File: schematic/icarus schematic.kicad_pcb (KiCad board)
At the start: 2 copper layers, 2 parts, among them U1 ESP32-S3, U2 BMI088

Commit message: added datasheets
other Datasheets

Added capacitors across motors

Added connectors instead of motors.

Add link to mini 100 brushed frame model

Remove URL from Frame file

Update Frame

Delete Frame

Add files via upload

this is the version -1 drone frame

PCB first iteration.
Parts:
- removed U1: ESP32-S3, Package_DFN_QFN:QFN-56-1EP_7x7mm_P0.4mm_EP4x4mm
- added C1: 10uF, Capacitor_SMD:C_0402_1005Metric_Pad0.74x0.62mm_HandSolder, F.Cu at (186.4, 96.0)
- added C10: 0.1uF, Capacitor_SMD:C_0603_1608Metric_Pad1.08x0.95mm_HandSolder, F.Cu at (219.9, 73.0)
- added C11: 0.1uF, Capacitor_SMD:C_0603_1608Metric_Pad1.08x0.95mm_HandSolder, F.Cu at (220.1, 95.5)
- added C12: 0.1uF, Capacitor_SMD:C_0603_1608Metric_Pad1.08x0.95mm_HandSolder, F.Cu at (220.2, 85.8)
- added C13: 0.1uF, Capacitor_SMD:C_0603_1608Metric_Pad1.08x0.95mm_HandSolder, F.Cu at (219.9, 79.3)
- added C2: 0.1uF, Capacitor_SMD:C_0402_1005Metric_Pad0.74x0.62mm_HandSolder, F.Cu at (183.9, 111.8)
- added C3: 10uF, Capacitor_SMD:C_0402_1005Metric_Pad0.74x0.62mm_HandSolder, F.Cu at (179.4, 96.0)
- added C4: 0.1uF, Capacitor_SMD:C_0402_1005Metric_Pad0.74x0.62mm_HandSolder, F.Cu at (184.1, 121.2)
- added C5: 100nf, Capacitor_SMD:C_0402_1005Metric_Pad0.74x0.62mm_HandSolder, F.Cu at (178.8, 109.0)
- added C6: 100nf, Capacitor_SMD:C_0402_1005Metric_Pad0.74x0.62mm_HandSolder, F.Cu at (202.2, 101.0)
- added C7: 100nf, Capacitor_SMD:C_0402_1005Metric_Pad0.74x0.62mm_HandSolder, F.Cu at (183.0, 96.0)
- added C8: 470uF, Capacitor_SMD:C_0603_1608Metric_Pad1.08x0.95mm_HandSolder, F.Cu at (215.1, 104.0)
- added C9: 100nf, Capacitor_SMD:C_0402_1005Metric_Pad0.74x0.62mm_HandSolder, F.Cu at (178.5, 129.5)
- added D1: LED, LED_SMD:LED_0603_1608Metric_Pad1.05x0.95mm_HandSolder, F.Cu at (194.2, 101.1)
- added D2: 1N5819, Diode_SMD:D_0603_1608Metric_Pad1.05x0.95mm_HandSolder, F.Cu at (219.9, 76.0)
- added D3: 1N5819, Diode_SMD:D_0603_1608Metric_Pad1.05x0.95mm_HandSolder, F.Cu at (220.1, 82.3)
- added D4: 1N5819, Diode_SMD:D_0603_1608Metric_Pad1.05x0.95mm_HandSolder, F.Cu at (220.4, 88.8)
- added D5: 1N5819, Diode_SMD:D_0603_1608Metric_Pad1.05x0.95mm_HandSolder, F.Cu at (220.1, 92.5)
- added D6: SS14, Diode_SMD:D_SMA, F.Cu at (198.0, 116.0)
- added D7: SP0503BAHT, Package_TO_SOT_SMD:SOT-143, F.Cu at (208.0, 126.8)
- added J1: Conn_01x02_Socket, Connector_JST:JST_EH_B2B-EH-A_1x02_P2.50mm_Vertical, F.Cu at (217.5, 110.5)
- added J2: USB_C_Receptacle_USB2.0_16P, Connector_USB:USB_C_Receptacle_GCT_USB4105-xx-A_16P_TopMnt_Horizontal, F.Cu at (198.0, 127.0)
- added J3: Conn_01x02_Socket, Connector_JST:JST_EH_B2B-EH-A_1x02_P2.50mm_Vertical, F.Cu at (217.5, 116.2)
- added J4: Conn_01x02_Socket, Connector_JST:JST_EH_B2B-EH-A_1x02_P2.50mm_Vertical, F.Cu at (217.5, 121.8)
- added J5: Conn_01x02_Socket, Connector_JST:JST_EH_B2B-EH-A_1x02_P2.50mm_Vertical, F.Cu at (217.5, 127.8)
- added Q1: AO3400A, Package_TO_SOT_SMD:SOT-23, F.Cu at (214.9, 75.0)
- added Q2: AO3400A, Package_TO_SOT_SMD:SOT-23, F.Cu at (215.0, 81.2)
- added Q3: AO3400A, Package_TO_SOT_SMD:SOT-23, F.Cu at (215.2, 86.8)
- added Q4: AO3400A, Package_TO_SOT_SMD:SOT-23, F.Cu at (215.2, 93.5)
- added R1: 220ohm, Resistor_SMD:R_0402_1005Metric_Pad0.72x0.64mm_HandSolder, F.Cu at (175.6, 96.0)
- added R10: 10k, Resistor_SMD:R_0603_1608Metric_Pad0.98x0.95mm_HandSolder, F.Cu at (209.2, 88.8)
- added R11: 10k, Resistor_SMD:R_0603_1608Metric_Pad0.98x0.95mm_HandSolder, F.Cu at (209.3, 95.5)
- added R12: 10k, Resistor_SMD:R_0402_1005Metric_Pad0.72x0.64mm_HandSolder, F.Cu at (184.1, 129.5)
- added R13: 5.1k, Resistor_SMD:R_0402_1005Metric_Pad0.72x0.64mm_HandSolder, F.Cu at (195.4, 120.2)
- added R14: 5.1k, Resistor_SMD:R_0402_1005Metric_Pad0.72x0.64mm_HandSolder, F.Cu at (200.8, 120.2)
- added R2: 10k, Resistor_SMD:R_0402_1005Metric_Pad0.72x0.64mm_HandSolder, F.Cu at (178.6, 111.8)
- added R3: 10k, Resistor_SMD:R_0402_1005Metric_Pad0.72x0.64mm_HandSolder, F.Cu at (178.8, 121.2)
- added R4: 100, Resistor_SMD:R_0603_1608Metric_Pad0.98x0.95mm_HandSolder, F.Cu at (209.0, 73.0)
- added R5: 100, Resistor_SMD:R_0603_1608Metric_Pad0.98x0.95mm_HandSolder, F.Cu at (209.1, 79.3)
- added R6: 100, Resistor_SMD:R_0603_1608Metric_Pad0.98x0.95mm_HandSolder, F.Cu at (209.2, 85.8)
- added R7: 100, Resistor_SMD:R_0603_1608Metric_Pad0.98x0.95mm_HandSolder, F.Cu at (209.3, 92.5)
- added R8: 10k, Resistor_SMD:R_0603_1608Metric_Pad0.98x0.95mm_HandSolder, F.Cu at (209.0, 76.0)
- added R9: 10k, Resistor_SMD:R_0603_1608Metric_Pad0.98x0.95mm_HandSolder, F.Cu at (209.2, 82.3)
- added SW1: SW_Push(BOOt), Button_Switch_SMD:SW_Push_SPST_NO_Alps_SKRK, F.Cu at (180.9, 115.5)
- added SW2: SW_Push(EN), Button_Switch_SMD:SW_Push_SPST_NO_Alps_SKRK, F.Cu at (180.9, 124.2)
- added TP1: TestPoint, TestPoint:TestPoint_Pad_1.0x1.0mm, F.Cu at (204.0, 75.0)
- added TP2: TestPoint, TestPoint:TestPoint_Pad_1.0x1.0mm, F.Cu at (204.0, 81.2)
- added TP3: TestPoint, TestPoint:TestPoint_Pad_1.0x1.0mm, F.Cu at (204.0, 87.0)
- added TP4: TestPoint, TestPoint:TestPoint_Pad_1.0x1.0mm, F.Cu at (204.0, 93.2)
- added TP5: TestPoint, TestPoint:TestPoint_Pad_4.0x4.0mm, F.Cu at (220.2, 99.8)
- added TP6: TestPoint, TestPoint:TestPoint_Pad_4.0x4.0mm, F.Cu at (220.2, 105.5)
- added U3: AMS1117-3.3, Package_TO_SOT_SMD:SOT-223-3_TabPin2, F.Cu at (179.8, 103.0)
- added U4: ESP32-S3-WROOM-1, RF_Module:ESP32-S3-WROOM-1, F.Cu at (183.0, 77.8)
- moved U2 79.6 mm to (198.0, 101.0), turned to 90 degrees
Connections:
- U2 pad 10: unconnected-(U2-SDO2-Pad10) -> /SD02
- U2 pad 11: unconnected-(U2-VDDIO-Pad11) -> /3.3V
- U2 pad 12: unconnected-(U2-INT3-Pad12) -> /INT3
- U2 pad 14: unconnected-(U2-~{CSB1}-Pad14) -> /CSB1
- U2 pad 15: unconnected-(U2-SDO1-Pad15) -> /SD01
- U2 pad 16: unconnected-(U2-INT1-Pad16) -> /INT1
- U2 pad 2: Net-(U2-GNDA-Pad2) -> GND
- U2 pad 3: unconnected-(U2-VDD-Pad3) -> /3.3V
- U2 pad 4: Net-(U2-GNDA-Pad2) -> GND
- U2 pad 5: unconnected-(U2-~{CSB2}-Pad5) -> /CSB2
- U2 pad 6: unconnected-(U2-GNDIO-Pad6) -> GND
- U2 pad 7: unconnected-(U2-PS-Pad7) -> GND
- U2 pad 8: unconnected-(U2-SCK/SCL-Pad8) -> /SCK
- U2 pad 9: unconnected-(U2-SDI/SDA-Pad9) -> /SDI
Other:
- board outline added: 50 x 60.2 mm
- board text added: "J2"

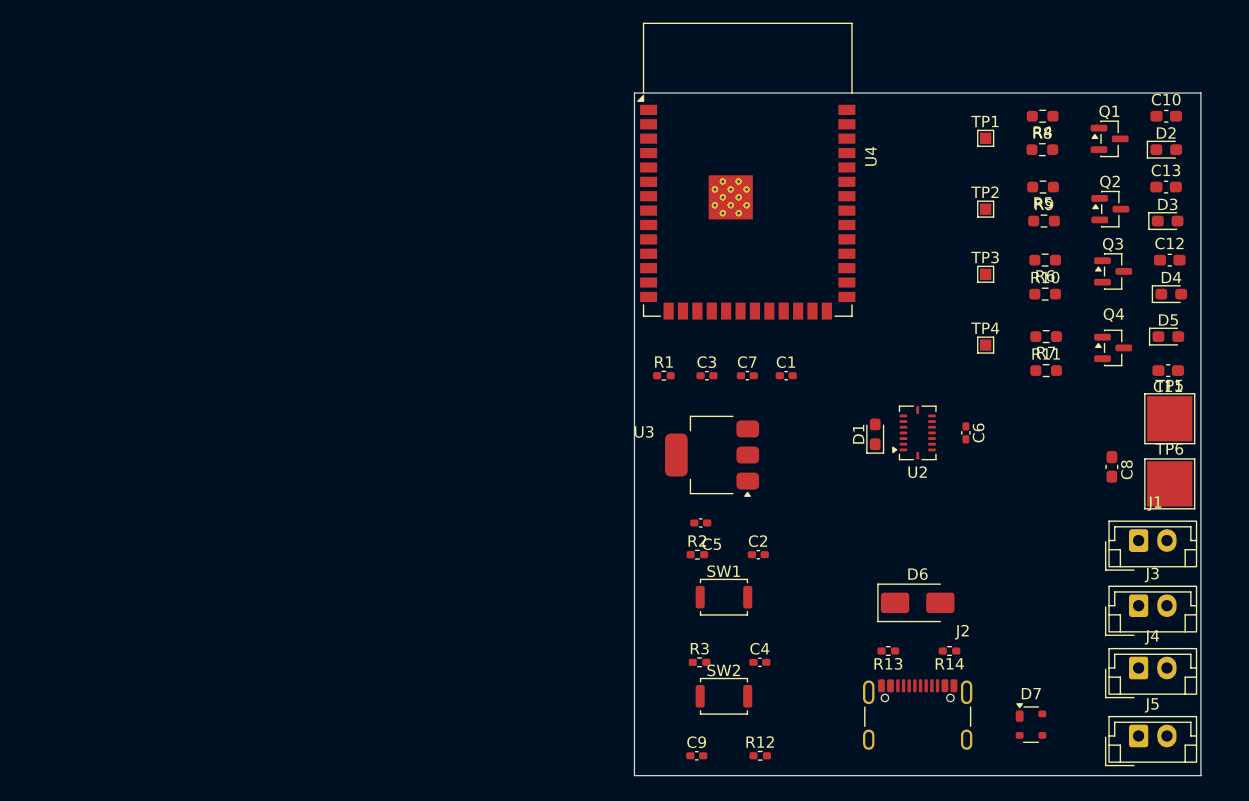
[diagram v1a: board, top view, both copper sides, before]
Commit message: Schematic change
Merge branch 'main' of https://github.com/Aryan2804/Icarus

Clean up lock files, add gitignore, track kicad project files

code for loadcell

code
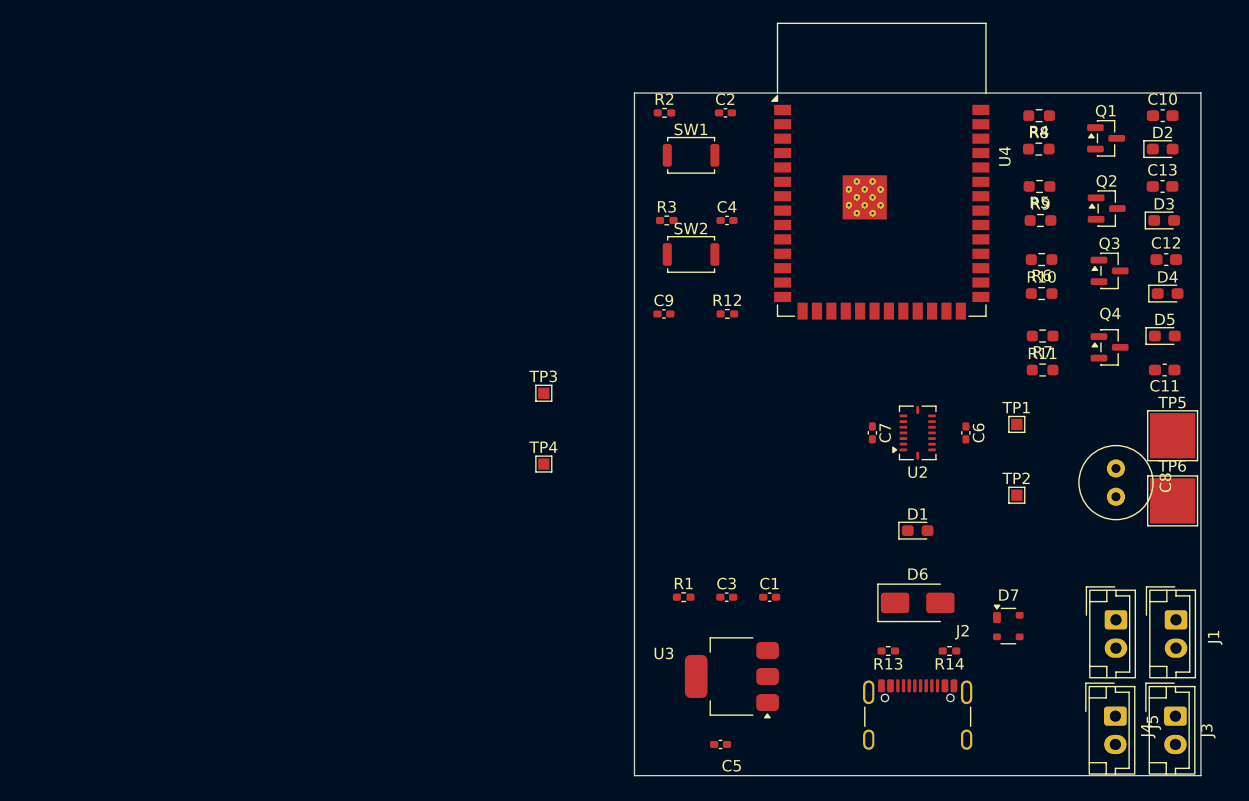
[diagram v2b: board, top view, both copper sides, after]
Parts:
- C8: footprint Capacitor_SMD:C_0603_1608Metric_Pad1.08x0.95mm_HandSolder -> Capacitor_THT:C_Radial_D6.3mm_H5.0mm_P2.50mm
- moved TP3 40.4 mm to (165.0, 97.5)
- moved TP4 40.4 mm to (165.0, 103.8)
- moved C2 39.1 mm to (181.0, 72.8)
- moved C4 39.1 mm to (181.2, 82.2)
- moved C9 39.1 mm to (175.6, 90.5)
- moved R12 39.1 mm to (181.2, 90.5)
- moved R2 39.1 mm to (175.7, 72.8)
- moved R3 39.1 mm to (175.8, 82.2)
- moved SW1 39.1 mm to (178.0, 76.5)
- moved SW2 39.1 mm to (178.0, 85.2)
- moved TP1 25.4 mm to (206.8, 100.2)
- moved TP2 25.4 mm to (206.8, 106.5)
- moved C3 19.6 mm to (181.1, 115.5)
- moved C5 19.6 mm to (180.6, 128.5)
- moved R1 19.6 mm to (177.3, 115.5)
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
